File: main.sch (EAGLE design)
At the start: 49 parts, among them IC1 MEGA8-AI, IC2 MCP73831, IC3 7805DT, Q2 32768k

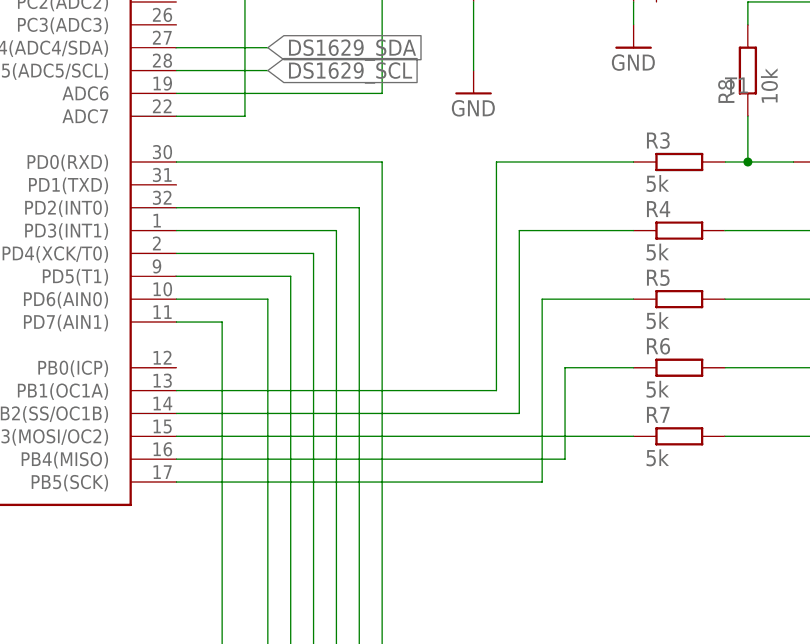
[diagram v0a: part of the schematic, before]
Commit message: Shift digit common pins Fix digit common pins
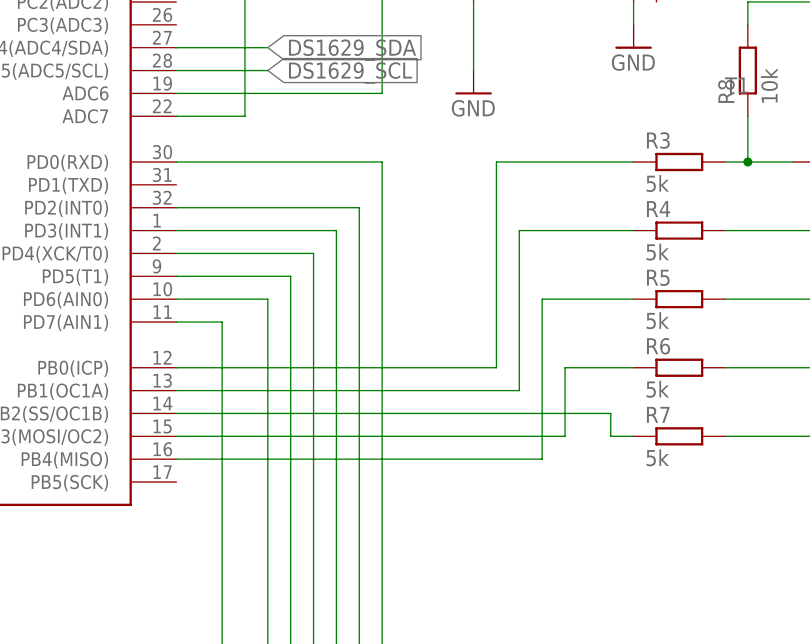
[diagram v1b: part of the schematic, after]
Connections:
- net N$23: now also IC1.PB0(ICP); no longer IC1.PB1(OC1A)
- net N$24: now also IC1.PB1(OC1A); no longer IC1.PB2(SS/OC1B)
- net N$25: now also IC1.PB4(MISO); no longer IC1.PB5(SCK)
- net N$26: now also IC1.PB3(MOSI/OC2); no longer IC1.PB4(MISO)
- net N$27: now also IC1.PB2(SS/OC1B); no longer IC1.PB3(MOSI/OC2)
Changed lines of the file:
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@@
 <segment>
 <wire x1="228.6" y1="129.54" x2="243.84" y2="129.54" width="0.1524" layer="91"/>
-<wire x1="193.04" y1="104.14" x2="228.6" y2="104.14" width="0.1524" layer="91"/>
-<wire x1="228.6" y1="104.14" x2="228.6" y2="129.54" width="0.1524" layer="91"/>
+<wire x1="228.6" y1="106.68" x2="228.6" y2="129.54" width="0.1524" layer="91"/>
+<pinref part="R3" gate="G$1" pin="1"/>
+<pinref part="IC1" gate="G$1" pin="PB0(ICP)"/>
+<wire x1="228.6" y1="106.68" x2="193.04" y2="106.68" width="0.1524" layer="91"/>
+</segment>
+</net>
+<net name="N$24" class="0">
+<segment>
+<wire x1="231.14" y1="104.14" x2="231.14" y2="121.92" width="0.1524" layer="91"/>
+<wire x1="231.14" y1="121.92" x2="243.84" y2="121.92" width="0.1524" layer="91"/>
+<pinref part="R4" gate="G$1" pin="1"/>
 <pinref part="IC1" gate="G$1" pin="PB1(OC1A)"/>
-<pinref part="R3" gate="G$1" pin="1"/>
-</segment>
-</net>
-<net name="N$24" class="0">
-<segment>
-<wire x1="193.04" y1="101.6" x2="231.14" y2="101.6" width="0.1524" layer="91"/>
-<wire x1="231.14" y1="101.6" x2="231.14" y2="121.92" width="0.1524" layer="91"/>
-<wire x1="231.14" y1="121.92" x2="243.84" y2="121.92" width="0.1524" layer="91"/>
-<pinref part="IC1" gate="G$1" pin="PB2(SS/OC1B)"/>
-<pinref part="R4" gate="G$1" pin="1"/>
+<wire x1="231.14" y1="104.14" x2="193.04" y2="104.14" width="0.1524" layer="91"/>
 </segment>
 </net>
 <net name="N$25" class="0">
 <segment>
-<wire x1="233.68" y1="93.98" x2="233.68" y2="114.3" width="0.1524" layer="91"/>
+<wire x1="233.68" y1="96.52" x2="233.68" y2="114.3" width="0.1524" layer="91"/>
 <wire x1="233.68" y1="114.3" x2="243.84" y2="114.3" width="0.1524" layer="91"/>
 <pinref part="R5" gate="G$1" pin="1"/>
-<pinref part="IC1" gate="G$1" pin="PB5(SCK)"/>
-<wire x1="233.68" y1="93.98" x2="193.04" y2="93.98" width="0.1524" layer="91"/>
+<pinref part="IC1" gate="G$1" pin="PB4(MISO)"/>
+<wire x1="233.68" y1="96.52" x2="193.04" y2="96.52" width="0.1524" layer="91"/>
 </segment>
 </net>
 <net name="N$26" class="0">
 <segment>
-<wire x1="193.04" y1="96.52" x2="236.22" y2="96.52" width="0.1524" layer="91"/>
-<wire x1="236.22" y1="96.52" x2="236.22" y2="106.68" width="0.1524" layer="91"/>
+<wire x1="236.22" y1="99.06" x2="236.22" y2="106.68" width="0.1524" layer="91"/>
 <wire x1="236.22" y1="106.68" x2="243.84" y2="106.68" width="0.1524" layer="91"/>
-<pinref part="IC1" gate="G$1" pin="PB4(MISO)"/>
 <pinref part="R6" gate="G$1" pin="1"/>
-</segment>
-</net>
-<net name="N$27" class="0">
-<segment>
-<pinref part="R7" gate="G$1" pin="1"/>
 <pinref part="IC1" gate="G$1" pin="PB3(MOSI/OC2)"/>
-<wire x1="243.84" y1="99.06" x2="193.04" y2="99.06" width="0.1524" layer="91"/>
+<wire x1="236.22" y1="99.06" x2="193.04" y2="99.06" width="0.1524" layer="91"/>
 </segment>
 </net>
@@
 </segment>
 </net>
+<net name="N$27" class="0">
+<segment>
+<pinref part="R7" gate="G$1" pin="1"/>
+<wire x1="243.84" y1="99.06" x2="241.3" y2="99.06" width="0.1524" layer="91"/>
+<wire x1="241.3" y1="99.06" x2="241.3" y2="101.6" width="0.1524" layer="91"/>
+<pinref part="IC1" gate="G$1" pin="PB2(SS/OC1B)"/>
+<wire x1="241.3" y1="101.6" x2="193.04" y2="101.6" width="0.1524" layer="91"/>
+</segment>
+</net>

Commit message: Schematics and PCB
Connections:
- net N$19: now also IC1.PD6(AIN0); no longer IC1.PD5(T1)
- net N$24: now also IC1.PB5(SCK)
- net N$28: now also Q2.1; no longer Q2.2
- net N$29: now also Q2.2; no longer Q2.1
- net N$3: now also IC1.ADC6; no longer IC1.ADC7
- net N$30: now also IC1.PD1(TXD)
- net N$35: now also IC1.PD5(T1); no longer IC1.PD6(AIN0)
- net N$38: now also IC1.PC0(ADC0); no longer IC1.ADC6
- net N$4: now also IC1.PC1(ADC1); no longer IC1.PC0(ADC0)
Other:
- moved on the sheet: Q2
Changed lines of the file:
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@@
 <instance part="GND5" gate="1" x="114.3" y="195.58"/>
 <instance part="LED1" gate="G$1" x="314.96" y="68.58"/>
-<instance part="Q2" gate="G$1" x="289.56" y="185.42" rot="R90"/>
+<instance part="Q2" gate="G$1" x="289.56" y="185.42" rot="R270"/>
 <instance part="GND6" gate="1" x="307.34" y="172.72"/>
 <instance part="+3V1" gate="G$1" x="289.56" y="210.82"/>
@@
 <pinref part="R4" gate="G$1" pin="1"/>
 <pinref part="IC1" gate="G$1" pin="PB1(OC1A)"/>
-<wire x1="231.14" y1="104.14" x2="193.04" y2="104.14" width="0.1524" layer="91"/>
+<wire x1="231.14" y1="104.14" x2="195.58" y2="104.14" width="0.1524" layer="91"/>
+<pinref part="IC1" gate="G$1" pin="PB5(SCK)"/>
+<wire x1="195.58" y1="104.14" x2="193.04" y2="104.14" width="0.1524" layer="91"/>
+<wire x1="193.04" y1="93.98" x2="195.58" y2="93.98" width="0.1524" layer="91"/>
+<wire x1="195.58" y1="93.98" x2="195.58" y2="104.14" width="0.1524" layer="91"/>
+<junction x="195.58" y="104.14"/>
 </segment>
 </net>
@@
 <junction x="256.54" y="193.04"/>
 <pinref part="R24" gate="G$1" pin="1"/>
-</segment>
-</net>
-<net name="N$28" class="0">
-<segment>
-<pinref part="U$1" gate="G$1" pin="X1"/>
-<pinref part="Q2" gate="G$1" pin="2"/>
-<wire x1="281.94" y1="187.96" x2="289.56" y2="187.96" width="0.1524" layer="91"/>
-<wire x1="289.56" y1="187.96" x2="294.64" y2="187.96" width="0.1524" layer="91"/>
-<junction x="289.56" y="187.96"/>
-<pinref part="C5" gate="G$1" pin="1"/>
-</segment>
-</net>
-<net name="N$29" class="0">
-<segment>
-<pinref part="U$1" gate="G$1" pin="X2"/>
-<pinref part="Q2" gate="G$1" pin="1"/>
-<wire x1="281.94" y1="182.88" x2="289.56" y2="182.88" width="0.1524" layer="91"/>
-<wire x1="289.56" y1="182.88" x2="294.64" y2="182.88" width="0.1524" layer="91"/>
-<junction x="289.56" y="182.88"/>
-<pinref part="C8" gate="G$1" pin="1"/>
 </segment>
 </net>
@@
 <wire x1="208.28" y1="48.26" x2="208.28" y2="119.38" width="0.1524" layer="91"/>
 <pinref part="IC1" gate="G$1" pin="PD4(XCK/T0)"/>
-<wire x1="208.28" y1="119.38" x2="193.04" y2="119.38" width="0.1524" layer="91"/>
+<wire x1="208.28" y1="119.38" x2="198.12" y2="119.38" width="0.1524" layer="91"/>
 <pinref part="R16" gate="G$1" pin="1"/>
+<pinref part="IC1" gate="G$1" pin="PD1(TXD)"/>
+<wire x1="198.12" y1="119.38" x2="193.04" y2="119.38" width="0.1524" layer="91"/>
+<wire x1="193.04" y1="127" x2="198.12" y2="127" width="0.1524" layer="91"/>
+<wire x1="198.12" y1="127" x2="198.12" y2="119.38" width="0.1524" layer="91"/>
+<junction x="198.12" y="119.38"/>
 </segment>
 </net>
@@
 <segment>
 <wire x1="205.74" y1="43.18" x2="241.3" y2="43.18" width="0.1524" layer="91"/>
-<wire x1="205.74" y1="43.18" x2="205.74" y2="116.84" width="0.1524" layer="91"/>
+<wire x1="205.74" y1="43.18" x2="205.74" y2="114.3" width="0.1524" layer="91"/>
+<pinref part="R17" gate="G$1" pin="1"/>
+<pinref part="IC1" gate="G$1" pin="PD6(AIN0)"/>
+<wire x1="205.74" y1="114.3" x2="193.04" y2="114.3" width="0.1524" layer="91"/>
+</segment>
+</net>
+<net name="N$35" class="0">
+<segment>
+<wire x1="203.2" y1="38.1" x2="241.3" y2="38.1" width="0.1524" layer="91"/>
+<wire x1="203.2" y1="38.1" x2="203.2" y2="116.84" width="0.1524" layer="91"/>
+<pinref part="R18" gate="G$1" pin="1"/>
 <pinref part="IC1" gate="G$1" pin="PD5(T1)"/>
-<wire x1="205.74" y1="116.84" x2="193.04" y2="116.84" width="0.1524" layer="91"/>
-<pinref part="R17" gate="G$1" pin="1"/>
-</segment>
-</net>
-<net name="N$35" class="0">
-<segment>
-<wire x1="203.2" y1="38.1" x2="241.3" y2="38.1" width="0.1524" layer="91"/>
-<wire x1="203.2" y1="38.1" x2="203.2" y2="114.3" width="0.1524" layer="91"/>
-<pinref part="IC1" gate="G$1" pin="PD6(AIN0)"/>
-<wire x1="203.2" y1="114.3" x2="193.04" y2="114.3" width="0.1524" layer="91"/>
-<pinref part="R18" gate="G$1" pin="1"/>
+<wire x1="203.2" y1="116.84" x2="193.04" y2="116.84" width="0.1524" layer="91"/>
 </segment>
 </net>
@@
 <wire x1="218.44" y1="185.42" x2="218.44" y2="187.96" width="0.1524" layer="91"/>
 <wire x1="218.44" y1="187.96" x2="218.44" y2="190.5" width="0.1524" layer="91"/>
-<wire x1="193.04" y1="134.62" x2="200.66" y2="134.62" width="0.1524" layer="91"/>
-<wire x1="200.66" y1="134.62" x2="200.66" y2="187.96" width="0.1524" layer="91"/>
+<wire x1="200.66" y1="137.16" x2="200.66" y2="187.96" width="0.1524" layer="91"/>
 <wire x1="200.66" y1="187.96" x2="218.44" y2="187.96" width="0.1524" layer="91"/>
 <junction x="218.44" y="187.96"/>
@@
 <wire x1="226.06" y1="187.96" x2="226.06" y2="182.88" width="0.1524" layer="91"/>
 <pinref part="D2" gate="G$1" pin="C"/>
-<pinref part="IC1" gate="G$1" pin="ADC7"/>
 <pinref part="R20" gate="G$1" pin="1"/>
 <pinref part="R21" gate="G$1" pin="2"/>
+<pinref part="IC1" gate="G$1" pin="ADC6"/>
+<wire x1="200.66" y1="137.16" x2="193.04" y2="137.16" width="0.1524" layer="91"/>
 </segment>
 </net>
@@
 <wire x1="124.46" y1="218.44" x2="124.46" y2="170.18" width="0.1524" layer="91"/>
 <wire x1="124.46" y1="170.18" x2="195.58" y2="170.18" width="0.1524" layer="91"/>
-<wire x1="195.58" y1="170.18" x2="195.58" y2="152.4" width="0.1524" layer="91"/>
-<wire x1="195.58" y1="152.4" x2="193.04" y2="152.4" width="0.1524" layer="91"/>
-<pinref part="IC1" gate="G$1" pin="PC0(ADC0)"/>
+<wire x1="195.58" y1="170.18" x2="195.58" y2="149.86" width="0.1524" layer="91"/>
+<pinref part="IC1" gate="G$1" pin="PC1(ADC1)"/>
+<wire x1="195.58" y1="149.86" x2="193.04" y2="149.86" width="0.1524" layer="91"/>
 </segment>
 </net>
@@
 <wire x1="243.84" y1="162.56" x2="243.84" y2="160.02" width="0.1524" layer="91"/>
 <wire x1="243.84" y1="160.02" x2="243.84" y2="157.48" width="0.1524" layer="91"/>
-<wire x1="215.9" y1="160.02" x2="226.06" y2="160.02" width="0.1524" layer="91"/>
+<wire x1="208.28" y1="160.02" x2="226.06" y2="160.02" width="0.1524" layer="91"/>
 <junction x="243.84" y="160.02"/>
-<pinref part="IC1" gate="G$1" pin="ADC6"/>
 <wire x1="226.06" y1="160.02" x2="243.84" y2="160.02" width="0.1524" layer="91"/>
-<wire x1="215.9" y1="160.02" x2="215.9" y2="137.16" width="0.1524" layer="91"/>
-<wire x1="215.9" y1="137.16" x2="193.04" y2="137.16" width="0.1524" layer="91"/>
 <wire x1="226.06" y1="160.02" x2="226.06" y2="154.94" width="0.1524" layer="91"/>
 <junction x="226.06" y="160.02"/>
 <pinref part="R22" gate="G$1" pin="1"/>
 <pinref part="C1" gate="G$1" pin="1"/>
+<wire x1="208.28" y1="160.02" x2="208.28" y2="152.4" width="0.1524" layer="91"/>
+<pinref part="IC1" gate="G$1" pin="PC0(ADC0)"/>
+<wire x1="208.28" y1="152.4" x2="193.04" y2="152.4" width="0.1524" layer="91"/>
 </segment>
 </net>
@@
 </segment>
 </net>
+<net name="N$28" class="0">
+<segment>
+<pinref part="U$1" gate="G$1" pin="X1"/>
+<pinref part="Q2" gate="G$1" pin="1"/>
+<wire x1="281.94" y1="187.96" x2="289.56" y2="187.96" width="0.1524" layer="91"/>
+<pinref part="C5" gate="G$1" pin="1"/>
+<wire x1="289.56" y1="187.96" x2="294.64" y2="187.96" width="0.1524" layer="91"/>
+<junction x="289.56" y="187.96"/>
+</segment>
+</net>
+<net name="N$29" class="0">
+<segment>
+<pinref part="U$1" gate="G$1" pin="X2"/>
+<pinref part="Q2" gate="G$1" pin="2"/>
+<wire x1="281.94" y1="182.88" x2="289.56" y2="182.88" width="0.1524" layer="91"/>
+<pinref part="C8" gate="G$1" pin="1"/>
+<wire x1="289.56" y1="182.88" x2="294.64" y2="182.88" width="0.1524" layer="91"/>
+<junction x="289.56" y="182.88"/>
+</segment>
+</net>
